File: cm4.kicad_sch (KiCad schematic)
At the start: 52 parts, among them J2 PicoBlade_1x12_533981371_SMT, Q1 MMBT2222AM3T5G, U3 SN74LVC1G04DRY, U4 SN74HCS244, U5 PCA9641BSHP

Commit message: leds
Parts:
- J2: value PicoBlade_1x12_533981371_SMT -> PicoBlade_1x14_533981471_SMT; footprint Connector_PicoBlade_Molex:MOLEX_533981271 -> Connector_PicoBlade_Molex:MOLEX_533981471; symbol Connector_PicoBlade_Molex:PicoBlade_1x12_533981371_SMT -> Connector_PicoBlade_Molex:PicoBlade_1x14_533981471_SMT; MPN 533981271 -> 533981471
- R18, R19: value 120R -> 260R
- R4: value 750R -> 100R
- R5: value 330R -> 260R
- R6, R7, R8, R9: value 1k -> 260R
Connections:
- net CM4_+3.3V: now also J2.13 (Pin_13); no longer J2.11 (Pin_11)
- net GND: now also J2.14 (Pin_14); no longer J2.12 (Pin_12)
- net ~{EthLED1}: now also R7.2; no longer R7.1
- net ~{EthLED2}: now also R8.2; no longer R8.1
- net ~{EthLED3}: now also R9.2; no longer R9.1
- net ~{LED_EthLED1_CONN}: now also R7.1; no longer R7.2
- net ~{LED_EthLED2_CONN}: now also R8.1; no longer R8.2
- net ~{LED_EthLED3_CONN}: now also R9.1; no longer R9.2
- net ~{LED_PI_Activity_CONN}: now also R6.2; no longer R6.1
- net ~{LED_PWR_LED_BUFFERED_CONN}: now also R5.2; no longer R5.1
- net ~{PI_Activity}: now also R6.1; no longer R6.2
- net ~{PWR_LED_BUFFERED}: now also R5.1; no longer R5.2
- new net LED_+3.3V_OK_CONN: J2.11 (Pin_11)
- new net LED_+5V_OK_CONN: J2.12 (Pin_12)
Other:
- sheet CM4 PSU ports: added +12V_IN, +3.3V_CONTROL, +3.3V_OK, +5V_OK; removed +12V_A_IN, CONTROL_+3.3V
- note added: "260R for non-Blue @ 3.3V, 5mA 600R for non-Blue @ 5V, 5mA 100R for Blue @ 3.3V, 5mA 440R for Blue @ 5V, 5mA"
- note added: "R260 for non-Blue @ 3.3V, 5mA R600 for non-Blue @ 5V, 5mA R100 for Blue @ 3.3V, 5mA R440 for Blue @ 5V, 6mA"
- moved on the sheet: R5, R6, R7, R8, R9

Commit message: led changes
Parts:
- R18, R6: value 260R -> 240R
- R19: value 260R -> 60R
- R4: value 100R -> 60R
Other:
- note added: "Dialight: 260R for Red @ 3.3V, Vf=2V, If=5mA 240R for Yellowgreen @ 3.3V, Vf=2.1V, If=5mA 260R for Yellow @ 3.3V, Vf=2V, If=5mA 260R for Orange @ 3.3V, Vf=2V, If=5mA 60R for Blue @ 3.3V, Vf=3V, If=5mA 580R for Yellowgreen @ 5V, Vf=2.1V, If=5mA"
- note added: "LITEON: 260R for non-Blue @ 3.3V, 5mA 600R for non-Blue @ 5V, 5mA 100R for Blue @ 3.3V, 5mA 440R for Blue @ 5V, 5mA"
- note removed: "260R for non-Blue @ 3.3V, 5mA 600R for non-Blue @ 5V, 5mA 100R for Blue @ 3.3V, 5mA 440R for Blue @ 5V, 5mA"
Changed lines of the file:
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@@
     (stroke (width 0) (type solid) (color 0 0 0 0))
+  )
+  (polyline (pts (xy 306.705 558.165) (xy 342.265 544.195))
+    (stroke (width 0) (type default) (color 0 0 0 0))
   )
   (wire (pts (xy 335.28 331.47) (xy 317.5 331.47))
@@
     (effects (font (size 1.27 1.27)) (justify left bottom))
   )
+  (text "LITEON:\n260R for non-Blue @ 3.3V, 5mA\n600R for non-Blue @ 5V, 5mA\n\n100R for Blue @ 3.3V, 5mA\n440R for Blue @ 5V, 5mA\n\n"
+    (at 307.975 558.165 0)
+    (effects (font (size 1.27 1.27)) (justify left bottom))
+  )
   (text "100Ω Differential Pair" (at 222.25 327.66 180)
     (effects (font (size 1.27 1.27)) (justify right bottom))
@@
   (text "ALT3" (at 214.884 274.066 180)
     (effects (font (size 1.27 1.27)) (justify right bottom))
+  )
+  (text "Dialight:\n260R for Red @ 3.3V, Vf=2V, If=5mA\n240R for Yellowgreen @ 3.3V, Vf=2.1V, If=5mA\n260R for Yellow @ 3.3V, Vf=2V, If=5mA\n260R for Orange @ 3.3V, Vf=2V, If=5mA\n60R for Blue @ 3.3V, Vf=3V, If=5mA\n\n580R for Yellowgreen @ 5V, Vf=2.1V, If=5mA\n"
+    (at 234.315 559.435 0)
+    (effects (font (size 1.27 1.27)) (justify left bottom))
   )
   (text "Output" (at 632.46 237.49 0)
@@
     (effects (font (size 3 3)) (justify left bottom))
   )
-  (text "260R for non-Blue @ 3.3V, 5mA\n600R for non-Blue @ 5V, 5mA\n\n100R for Blue @ 3.3V, 5mA\n440R for Blue @ 5V, 5mA\n\n"
-    (at 268.605 556.26 0)
-    (effects (font (size 1.27 1.27)) (justify left bottom))
-  )
   (text "FIXME: USB hub and Coral TPU?" (at 675.64 288.29 0)
     (effects (font (size 5 5) (thickness 1) bold italic) (justify left bottom))
@@
       (effects (font (size 1.27 1.27)) (justify right))
     )
-    (property "Value" "260R" (id 1) (at 439.42 523.24 90)
+    (property "Value" "240R" (id 1) (at 439.42 523.24 90)
       (effects (font (size 1.27 1.27)) (justify left))
     )
@@
       (effects (font (size 1.27 1.27)) (justify right))
     )
-    (property "Value" "260R" (id 1) (at 635 524.51 90)
+    (property "Value" "60R" (id 1) (at 635 524.51 90)
       (effects (font (size 1.27 1.27)) (justify left))
     )
@@
       (effects (font (size 1.27 1.27)) (justify right))
     )
-    (property "Value" "100R" (id 1) (at 300.99 508 90)
+    (property "Value" "60R" (id 1) (at 300.99 508 90)
       (effects (font (size 1.27 1.27)) (justify left))
     )
@@
       (effects (font (size 1.27 1.27)) (justify right))
     )
-    (property "Value" "260R" (id 1) (at 635 506.73 90)
-      (effects (font (size 1.27 1.27)) (justify left))
-    )
+    (property "Value" "240R" (id 1) (at 635 506.73 90)
+      (effects (font (size 1.27 1.27)) (justify left))
+    )

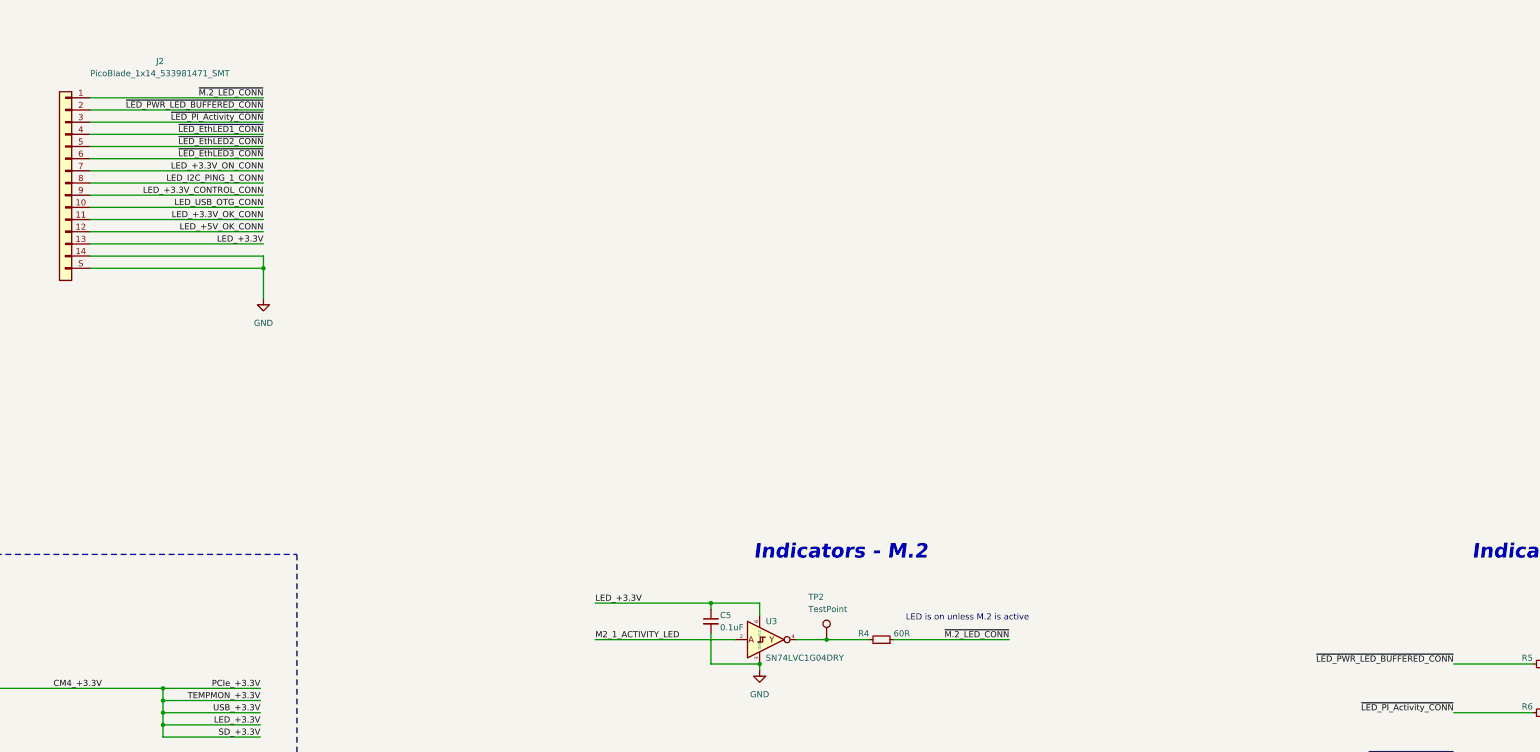
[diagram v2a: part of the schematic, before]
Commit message: trued up facecm4 connector pinout
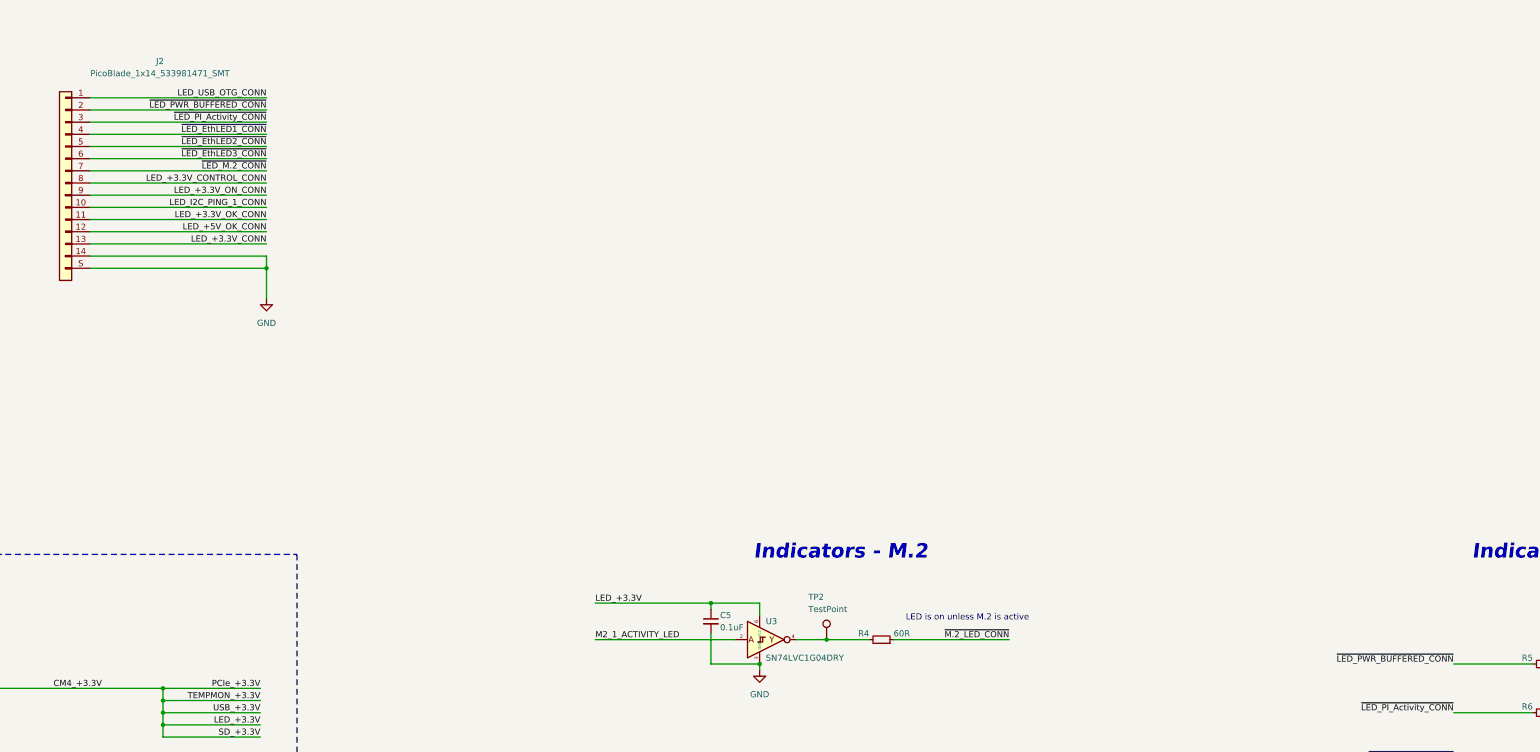
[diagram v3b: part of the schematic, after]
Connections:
- net +3.3V_CONTROL: now also J2.8 (Pin_8); no longer J2.9 (Pin_9)
- net CM4_+3.3V: no longer J2.13 (Pin_13)
- net LED_+3.3V_ON_CONN: now also J2.9 (Pin_9); no longer J2.7 (Pin_7)
- net LED_I2C_PING_1_CONN: now also J2.10 (Pin_10); no longer J2.8 (Pin_8)
- net LED_USB_OTG_CONN: now also J2.1 (Pin_1); no longer J2.10 (Pin_10)
- net ~{M.2_LED_CONN}: no longer J2.1 (Pin_1)
- net ~{LED_PWR_LED_BUFFERED_CONN} renamed ~{LED_PWR_BUFFERED_CONN}
- new net LED_+3.3V_CONN: J2.13 (Pin_13)
- new net ~{LED_M.2_CONN}: J2.7 (Pin_7)
